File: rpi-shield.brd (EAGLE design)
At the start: 160 x 100 mm, 35 parts

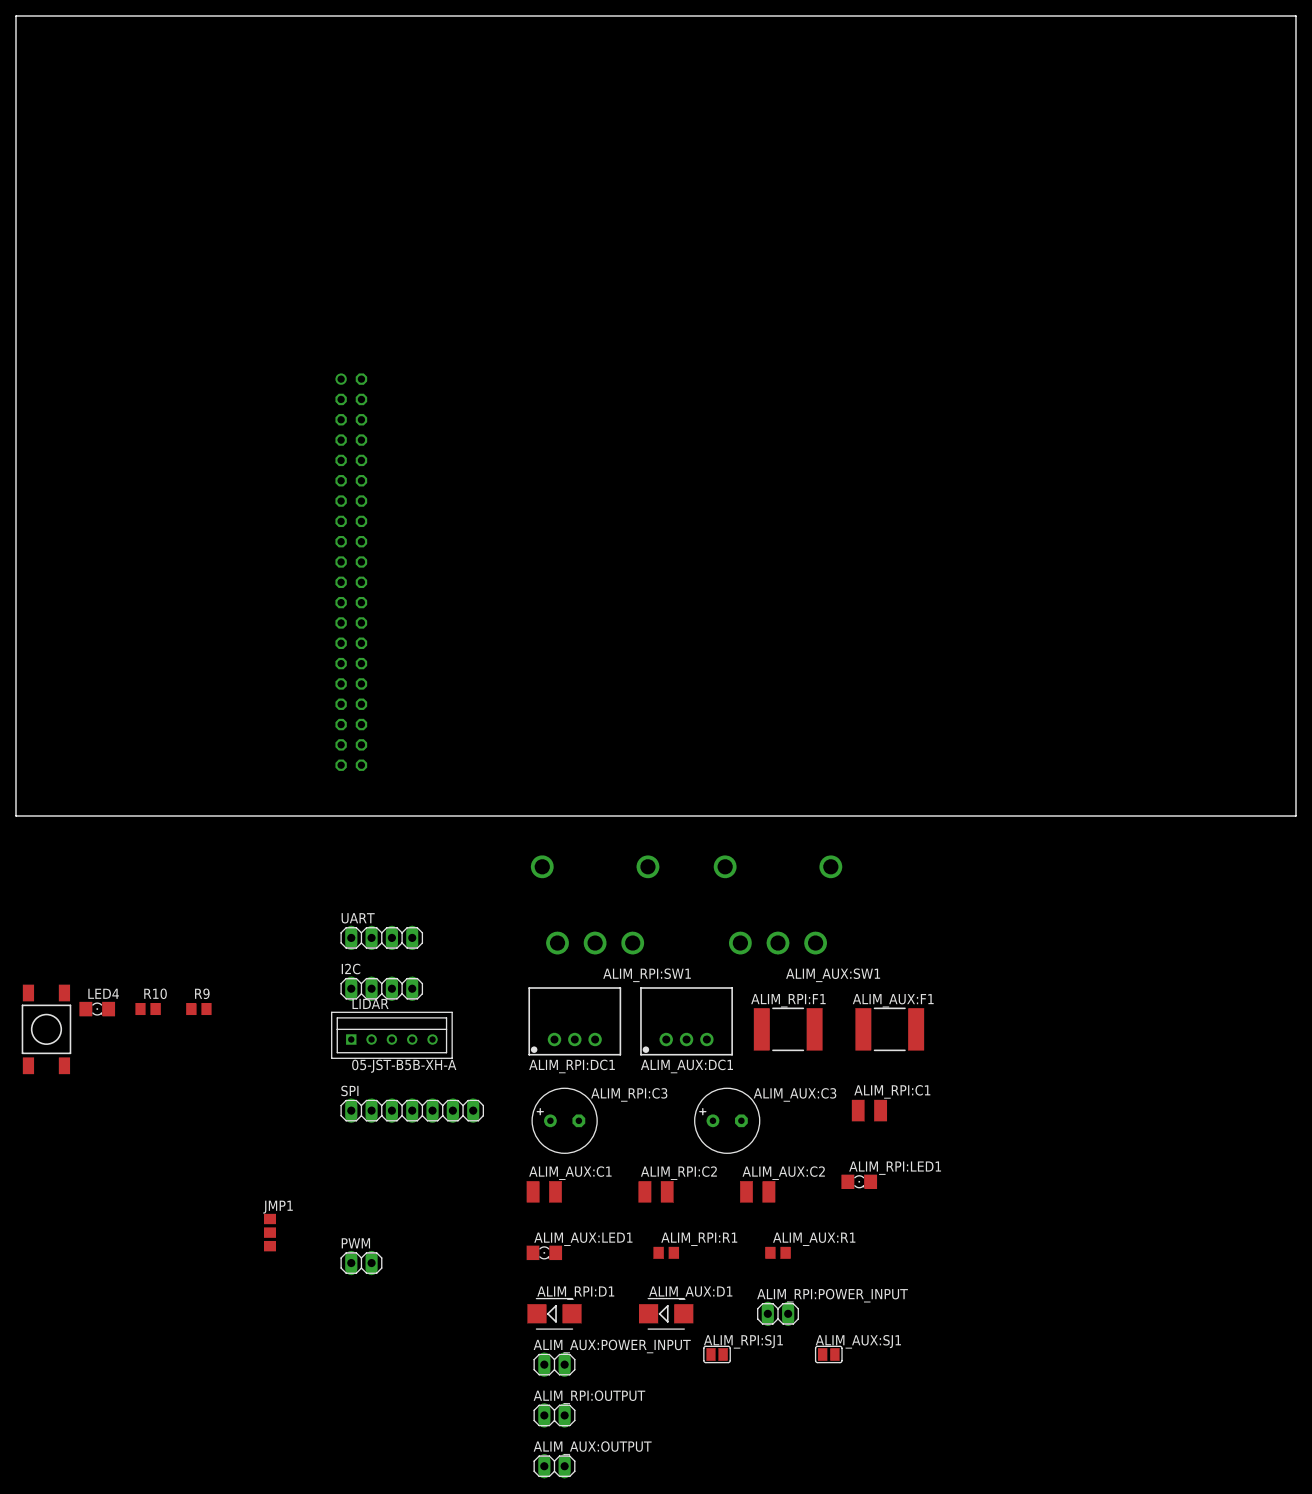
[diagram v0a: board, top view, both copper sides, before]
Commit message: placement composants rpi-shield
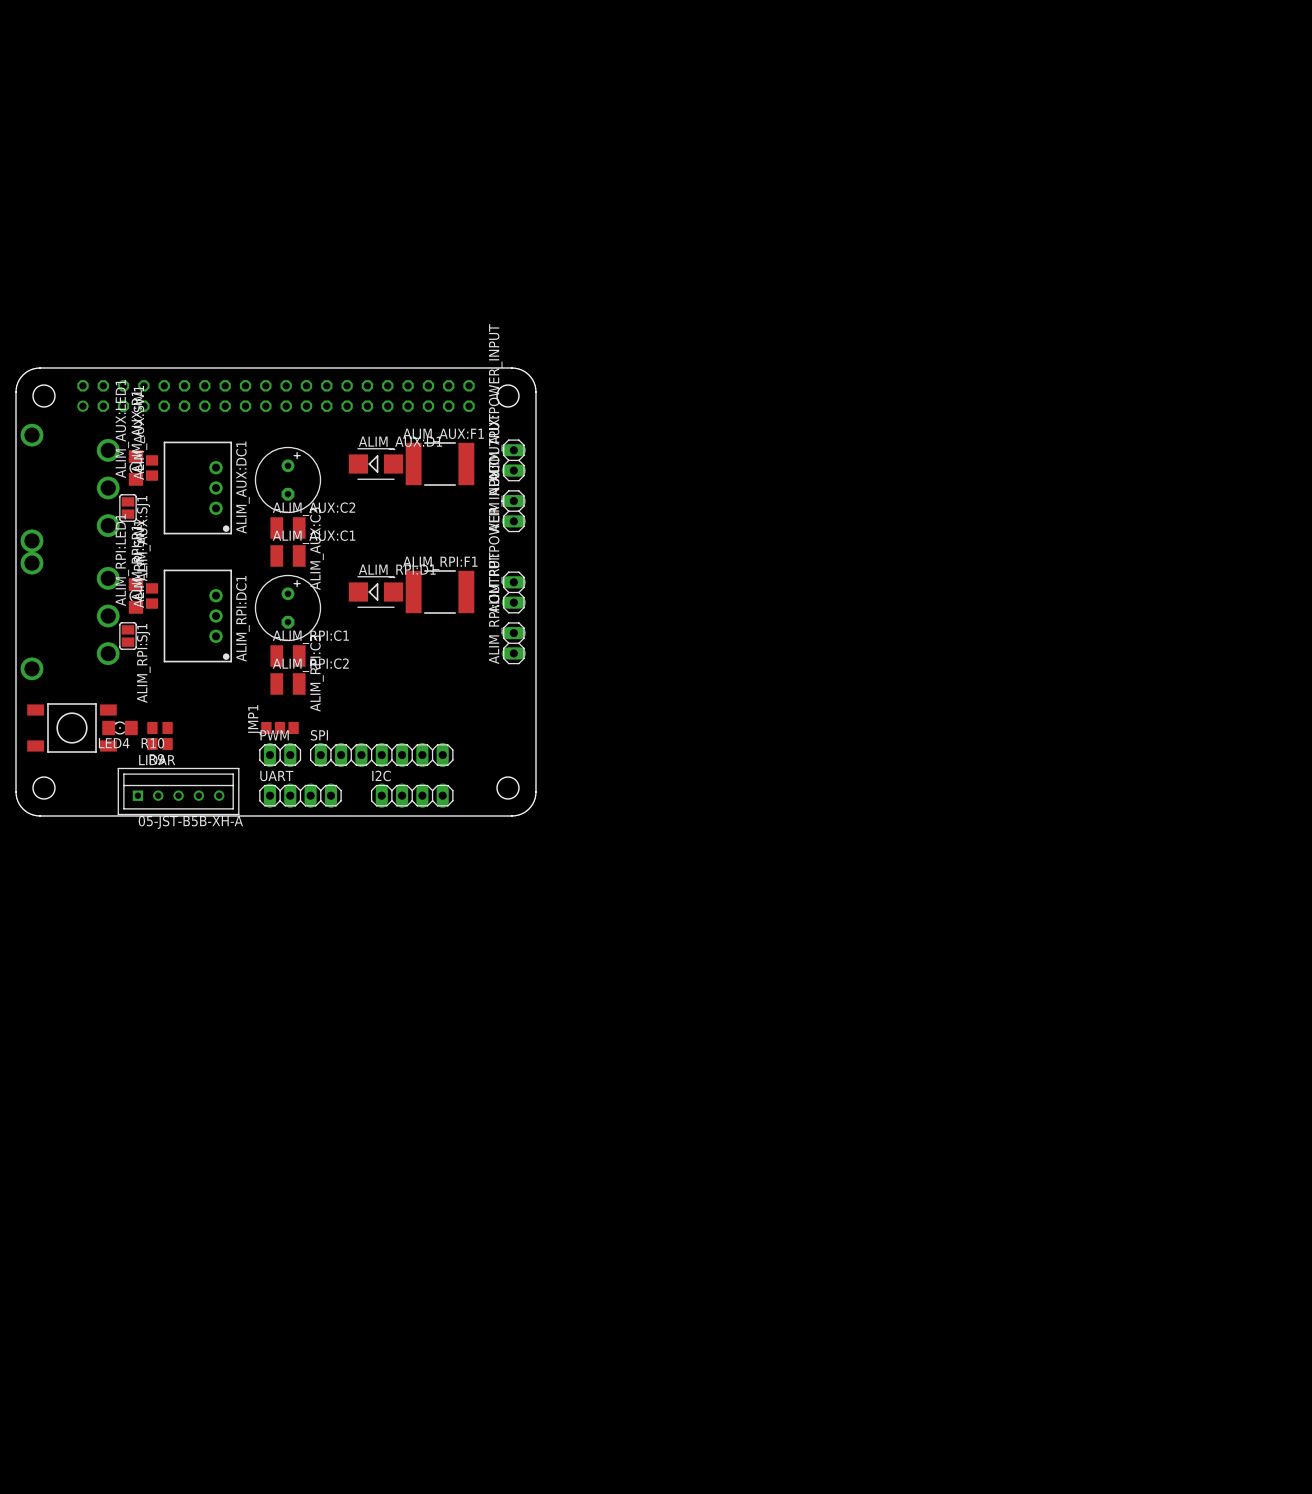
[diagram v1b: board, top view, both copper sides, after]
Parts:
- moved ALIM_AUX:SJ1 137.4 mm to (14.0, 38.5), turned to 270 degrees
- moved ALIM_AUX:R1 125.5 mm to (17.0, 43.5), turned to 90 degrees
- moved ALIM_AUX:OUTPUT 119.5 mm to (62.2, 38.1), turned to 90 degrees
- moved ALIM_RPI:LED1 116.3 mm to (15.0, 27.5), turned to 90 degrees
- moved ALIM_RPI:SJ1 116.1 mm to (14.0, 22.5), turned to 270 degrees
- moved ALIM_AUX:POWER_INPUT 113.1 mm to (62.2, 44.5), turned to 90 degrees
- moved ALIM_AUX:D1 112.3 mm to (45.0, 44.0)
- moved ALIM_AUX:LED1 110.6 mm to (15.0, 43.5), turned to 90 degrees
- moved ALIM_AUX:SW1 104.6 mm to (2.00, 41.0), turned to 90 degrees
- moved ALIM_RPI:R1 104.3 mm to (17.0, 27.5), turned to 90 degrees
- moved ALIM_AUX:C2 101.7 mm to (34.0, 36.0)
- moved ALIM_AUX:C3 97.1 mm to (34.0, 42.0), turned to 270 degrees
- moved ALIM_RPI:OUTPUT 96.7 mm to (62.2, 21.6), turned to 90 degrees
- moved ALIM_RPI:POWER_INPUT 96.0 mm to (62.2, 27.9), turned to 90 degrees
- moved ALIM_RPI:D1 92.9 mm to (45.0, 28.0)
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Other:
- board size 160 x 100 mm -> 65 x 56 mm

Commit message: all done, missing doc
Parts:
- moved R9 0.50 mm to (18.0, 8.50)
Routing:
- net +3V3: track 0.00 -> 136.7 mm
- net GND: track 0.00 -> 106.9 mm, vias 0 -> 2
- net +5V/1: track 0.00 -> 92.1 mm, vias 0 -> 1
- net +5V: track 0.00 -> 88.2 mm, vias 0 -> 1
- net N$2: track 0.00 -> 83.2 mm, vias 0 -> 1
- net SCL: track 0.00 -> 82.3 mm
- net SDA: track 0.00 -> 82.3 mm
- net TX: track 0.00 -> 76.9 mm, vias 0 -> 1
- net RX: track 0.00 -> 72.5 mm, vias 0 -> 1
- net PWM0: track 0.00 -> 65.2 mm, vias 0 -> 2
- net N$5: track 0.00 -> 65.2 mm, vias 0 -> 1
- net PWM1: track 0.00 -> 58.7 mm, vias 0 -> 1
- net CE1: track 0.00 -> 55.3 mm
- net CE0: track 0.00 -> 52.6 mm
- net MOSI: track 0.00 -> 48.6 mm
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- added copper zone on layer 1, net GND
- added copper zone on layer 16, net GND

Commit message: CAM files are ready
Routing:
- net GND: vias 2 -> 10
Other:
- board text added: "AUX"
- board text added: "AUX 5V"
- board text added: "CE0"
- board text added: "CE1"
- board text added: "GND"
- board text added: "I2C [SDA|SCL]"
- board text added: "MISO"
- board text added: "MOSI"
- board text added: "PWM"
- board text added: "RPI"
- board text added: "RPI 5V"
- board text added: "SCLK"
- board text added: "SPI"
- board text added: "UART [TX|RX]"
- board text added: "VIN"
- board text added: "© 2019 - GobGob Senpaï"
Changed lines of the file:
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@@
 <setting verticaltext="up"/>
 </settings>
-<grid distance="1" unitdist="mm" unit="mm" style="lines" multiple="1" display="yes" altdistance="0.5" altunitdist="mm" altunit="mm"/>
+<grid distance="1" unitdist="mm" unit="mm" style="lines" multiple="1" display="yes" altdistance="0.1" altunitdist="mm" altunit="mm"/>
 <layers>
 <layer number="1" name="Top" color="4" fill="1" visible="yes" active="yes"/>
@@
 <wire x1="62" y1="56" x2="3" y2="56" width="0" layer="20"/>
 <wire x1="3" y1="56" x2="0" y2="53" width="0" layer="20" curve="90"/>
-<hole x="3.5" y="3.5" drill="2.75"/>
-<hole x="61.5" y="3.5" drill="2.75"/>
-<hole x="3.5" y="52.5" drill="2.75"/>
-<hole x="61.5" y="52.5" drill="2.75"/>
+<text x="16" y="41" size="1.778" layer="21" rot="SR270">AUX</text>
+<text x="16" y="25" size="1.778" layer="21" rot="SR270">RPI</text>
+<text x="29.8" y="4.2" size="1.27" layer="21">UART [TX|RX]</text>
+<text x="44.4" y="4.2" size="1.27" layer="21">I2C [SDA|SCL]</text>
+<text x="38.1" y="9.5" size="1.27" layer="21">SPI</text>
+<text x="43.7" y="9.4" size="1.27" layer="21" rot="R90">MOSI</text>
+<text x="46.3" y="9.4" size="1.27" layer="21" rot="R90">MISO</text>
+<text x="48.9" y="9.4" size="1.27" layer="21" rot="R90">SCLK</text>
+<text x="51.4" y="9.4" size="1.27" layer="21" rot="R90">CE0</text>
+<text x="54" y="9.4" size="1.27" layer="21" rot="R90">CE1</text>
+<text x="26.2" y="8.4" size="1.27" layer="21">PWM</text>
+<text x="60.4" y="21.2" size="1.778" layer="21" rot="R180">RPI 5V</text>
+<text x="58.5" y="27.5" size="1.778" layer="21" rot="R270">GND</text>
+<text x="58.5" y="32.3" size="1.778" layer="21" rot="R270">VIN</text>
+<text x="58.5" y="44" size="1.778" layer="21" rot="R270">GND</text>
+<text x="58.5" y="49" size="1.778" layer="21" rot="R270">VIN</text>
+<text x="60.6" y="37.8" size="1.778" layer="21" rot="R180">AUX 5V</text>
+<wire x1="64" y1="44.4" x2="58" y2="44.4" width="0.1524" layer="21"/>
+<wire x1="58" y1="44.4" x2="58" y2="38.1" width="0.1524" layer="21"/>
+<wire x1="58" y1="38.1" x2="64" y2="38.1" width="0.1524" layer="21"/>
+<wire x1="64" y1="38.1" x2="64" y2="44.4" width="0.1524" layer="21"/>
+<wire x1="64" y1="27.9" x2="58" y2="27.9" width="0.1524" layer="21"/>
+<wire x1="58" y1="27.9" x2="58" y2="21.6" width="0.1524" layer="21"/>
+<wire x1="58" y1="21.6" x2="64" y2="21.6" width="0.1524" layer="21"/>
+<wire x1="64" y1="21.6" x2="64" y2="27.9" width="0.1524" layer="21"/>
+<rectangle x1="60.8" y1="38.1" x2="64" y2="44.4" layer="21"/>
+<rectangle x1="60.7" y1="21.6" x2="64" y2="27.9" layer="21"/>
+<rectangle x1="33" y1="0.2" x2="35.5" y2="4" layer="21"/>
+<rectangle x1="47" y1="0.2" x2="49.5" y2="4" layer="21"/>
+<rectangle x1="39.4" y1="5.6" x2="41.9" y2="9.1" layer="21"/>
+<text x="57" y="50" size="1.778" layer="21" rot="R180">© 2019 - GobGob Senpaï</text>
 </plain>
 <attributes>
@@
 </element>
 <element name="LIDAR" library="bt_con-jst-xh" package="B5B-XH" value="05-JST-B5B-XH-A" x="20.32" y="2.54" smashed="yes">
-<attribute name="NAME" x="15.24" y="6.35" size="1.27" layer="21"/>
-<attribute name="VALUE" x="15.24" y="-1.27" size="1.27" layer="21"/>
+<attribute name="NAME" x="20.24" y="6.35" size="1.27" layer="21"/>
 </element>
 <element name="SPI" library="pinhead" library_urn="urn:adsk.eagle:library:325" package="1X07" package3d_urn="urn:adsk.eagle:package:22477/2" value="" x="45.72" y="7.62" smashed="yes">
@@
 <vertex x="0" y="0"/>
 </polygon>
+<via x="25" y="13" extent="1-16" drill="0.35"/>
+<via x="30" y="13" extent="1-16" drill="0.35"/>
+<via x="30" y="16" extent="1-16" drill="0.35"/>
+<via x="25" y="16" extent="1-16" drill="0.35"/>
+<via x="3.5" y="52.5" extent="1-16" drill="2.75" diameter="5" shape="octagon"/>
+<via x="61.5" y="52.5" extent="1-16" drill="2.75" diameter="5" shape="octagon"/>
+<via x="61.5" y="3.5" extent="1-16" drill="2.75" diameter="5" shape="octagon"/>
+<via x="3.5" y="3.5" extent="1-16" drill="2.75" diameter="5" shape="octagon"/>
 </signal>
 <signal name="+3V3">
@@
 <wire x1="57" y1="24.6" x2="37.178" y2="24.6" width="0.8" layer="1"/>
 <wire x1="25" y1="27.54" x2="19.54" y2="33" width="0.8" layer="16"/>
-<wire x1="6.4" y1="51.8" x2="8.37" y2="53.77" width="0.8" layer="16"/>
 <wire x1="17.2" y1="33" x2="9.6" y2="33" width="0.8" layer="16"/>
-<wire x1="9.6" y1="33" x2="6.4" y2="36.2" width="0.8" layer="16"/>
-<wire x1="6.4" y1="36.2" x2="6.4" y2="51.8" width="0.8" layer="16"/>
 <wire x1="8.37" y1="53.77" x2="10.91" y2="53.77" width="0.8" layer="16"/>
 <wire x1="19.54" y1="33" x2="17.2" y2="33" width="0.8" layer="16"/>
@@
 <wire x1="17" y1="28.45" x2="17.2" y2="28.65" width="0.3" layer="1"/>
 <wire x1="17.2" y1="28.65" x2="17.2" y2="33" width="0.3" layer="1"/>
+<wire x1="9.6" y1="33" x2="7" y2="35.6" width="0.8" layer="16"/>
+<wire x1="7" y1="52.4" x2="8.37" y2="53.77" width="0.8" layer="16"/>
+<wire x1="7" y1="35.6" x2="7" y2="52.4" width="0.8" layer="16"/>
 </signal>
 <signal name="TX">
